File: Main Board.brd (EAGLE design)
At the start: 37.3 x 95 mm, 55 parts, among them IC1 ATSAMD21G18A-AF, IC2 BMP388, IC3 CAT24C64WI-GT3, IC4 DRV2605, IC5 AP63205WU-7, IC8 AP2114H-3.3TRG1, J1 10118194-0001LF, J2 BM06B-SRSS-TB(LF)(SN), Q1 BC817-25LT1SMD, Y1 ECS-.327-7-34B-TR

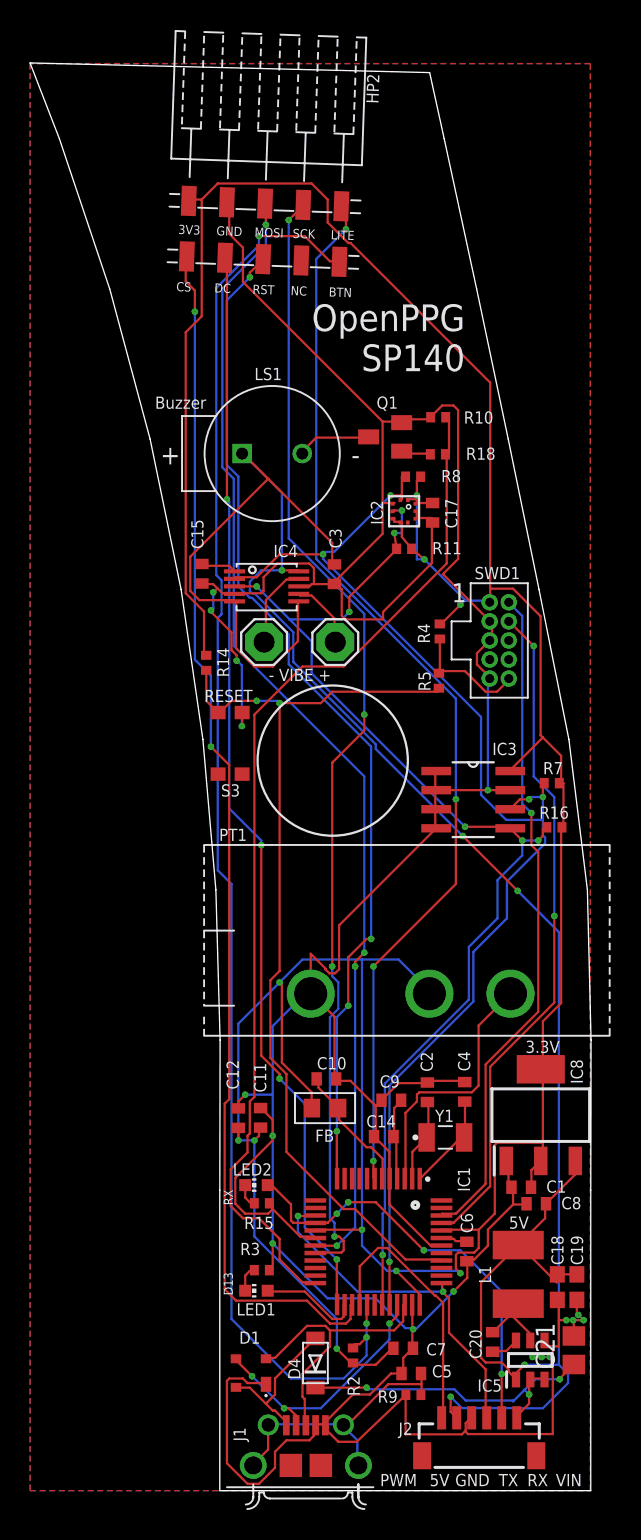
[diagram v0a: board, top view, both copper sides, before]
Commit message: fixed C21 tplace silkscreen, fixed esc connector silkscreen spacing, fixed too big 0402 cap footprints
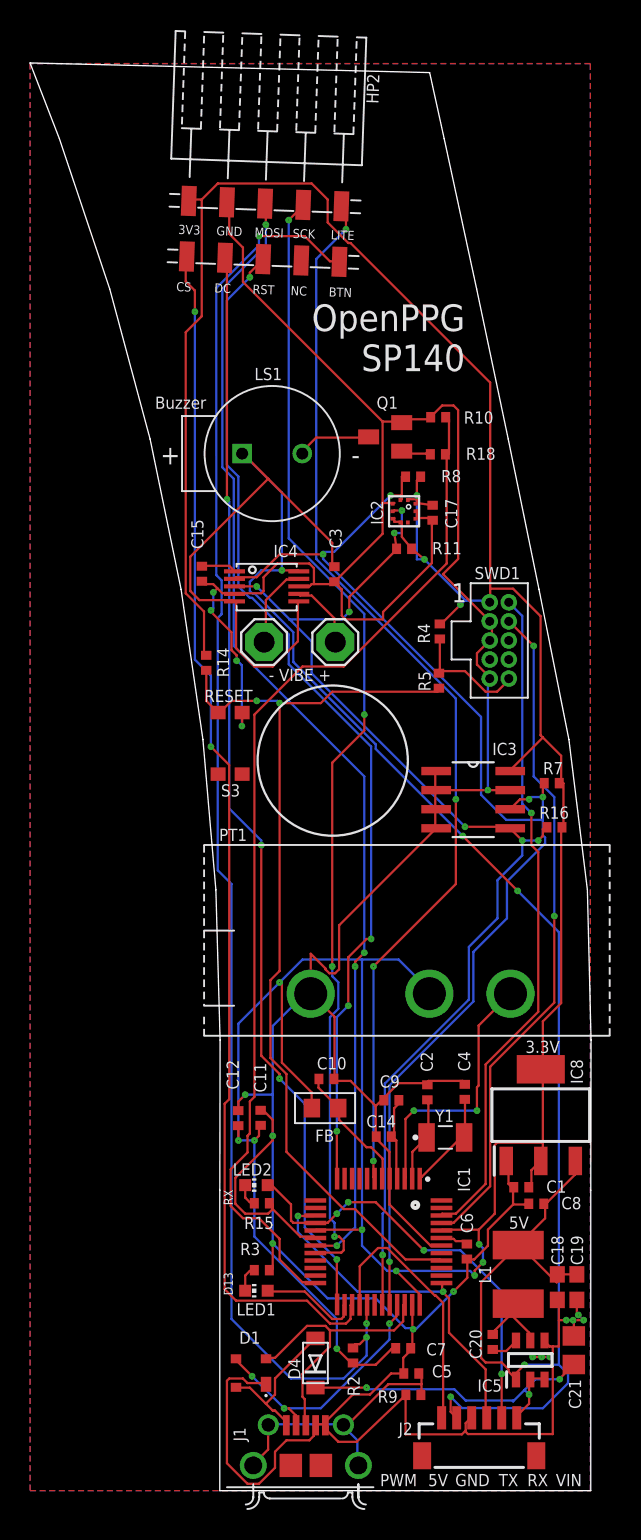
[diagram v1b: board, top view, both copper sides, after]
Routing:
- net GND: track 291.7 -> 293.0 mm
- net 3.3V: track 245.7 -> 246.3 mm, vias 10 -> 12
- net A0_POT: track 17.3 -> 17.7 mm, vias 0 -> 2

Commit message: Rx and Tx to pin 37 and 38; Shifted location of JST; Added holes for zip tie
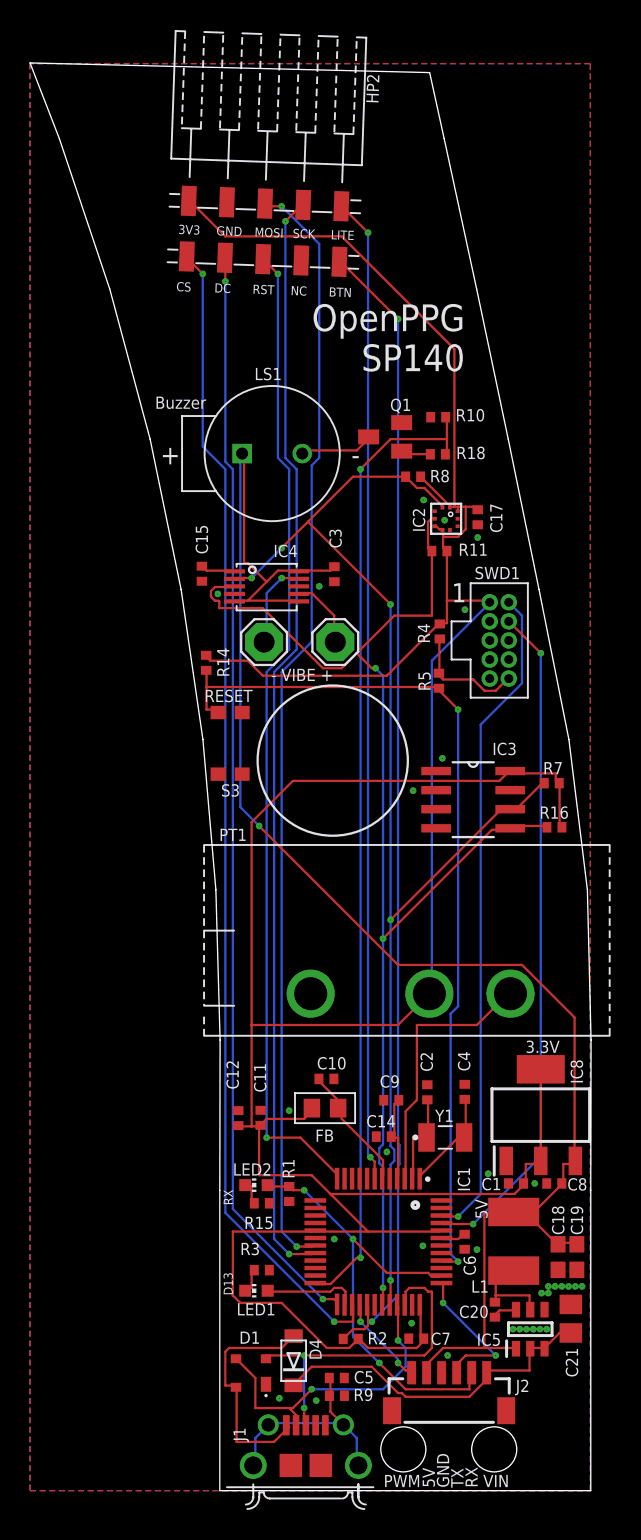
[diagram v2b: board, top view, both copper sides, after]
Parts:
- added R1: 1k, rcl:R0402
- moved R9 5.09 mm to (20.4, 6.32), turned to 180 degrees
- moved C5 4.97 mm to (20.4, 7.50), turned to 0 degrees
- moved J2 3.61 mm to (27.9, 6.20)
- moved C17 3.01 mm to (29.8, 64.8)
- moved IC2 2.84 mm to (27.7, 64.7)
- moved R11 2.35 mm to (27.2, 62.5)
- moved L1 2.22 mm to (32.2, 16.6)
- moved C20 2.16 mm to (30.9, 12.1)
- moved C21 2.11 mm to (36.0, 11.4)
- moved IC5 2.05 mm to (33.3, 10.8)
- moved C18 2.00 mm to (35.1, 15.6)
- moved C19 2.00 mm to (36.4, 15.6)
- moved C8 1.81 mm to (34.9, 20.4)
- moved D4 1.46 mm to (17.6, 8.65)
- moved R2 1.11 mm to (21.4, 10.1), turned to 180 degrees
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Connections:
- net GND: now also R1.2
- net RX0_FROM_ESC: now also IC1.38, R1.1; no longer IC1.16
- net TX1_TO_ESC: no longer IC1.15
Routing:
- net GND: track 293.0 -> 0.00 mm, vias 17 -> 33
- net 5V: track 147.2 -> 111.2 mm, vias 5 -> 1
- net D6_BTN: track 95.9 -> 76.7 mm, vias 3 -> 2
- net 3.3V: track 246.3 -> 230.3 mm, vias 12 -> 0
- net TX1_TO_ESC: track 23.8 -> 9.72 mm
- net D12_TO_ESC: track 17.8 -> 6.09 mm, vias 0 -> 2
- net SDA: track 77.8 -> 86.2 mm, vias 8 -> 3
- net A1_TFTLITE: track 71.8 -> 65.7 mm, vias 4 -> 2
- net VBUS: track 10.3 -> 15.7 mm
- net SH: track 19.1 -> 15.0 mm
- net D+: track 18.7 -> 22.7 mm, vias 0 -> 2
- net SCL: track 82.3 -> 86.2 mm
- net D5_BUZ: track 69.0 -> 65.4 mm, vias 0 -> 2
- net RST: track 62.6 -> 59.3 mm
- net D10_TFTCS: track 80.6 -> 77.3 mm
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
